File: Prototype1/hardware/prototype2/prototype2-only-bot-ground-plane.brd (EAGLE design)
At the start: 96.6 x 74.9 mm, 94 parts, among them IC1 ATTINY13A-SSU, IC2 LDL112D33R, IC3 FT2232HL-REEL, IC4 93LC46BT-I_OT, IC5 APA104, IC6 APA104, IC7 APA104, IC8 APA104, J4 DN PAIR, U2 ESP-WROOM-32

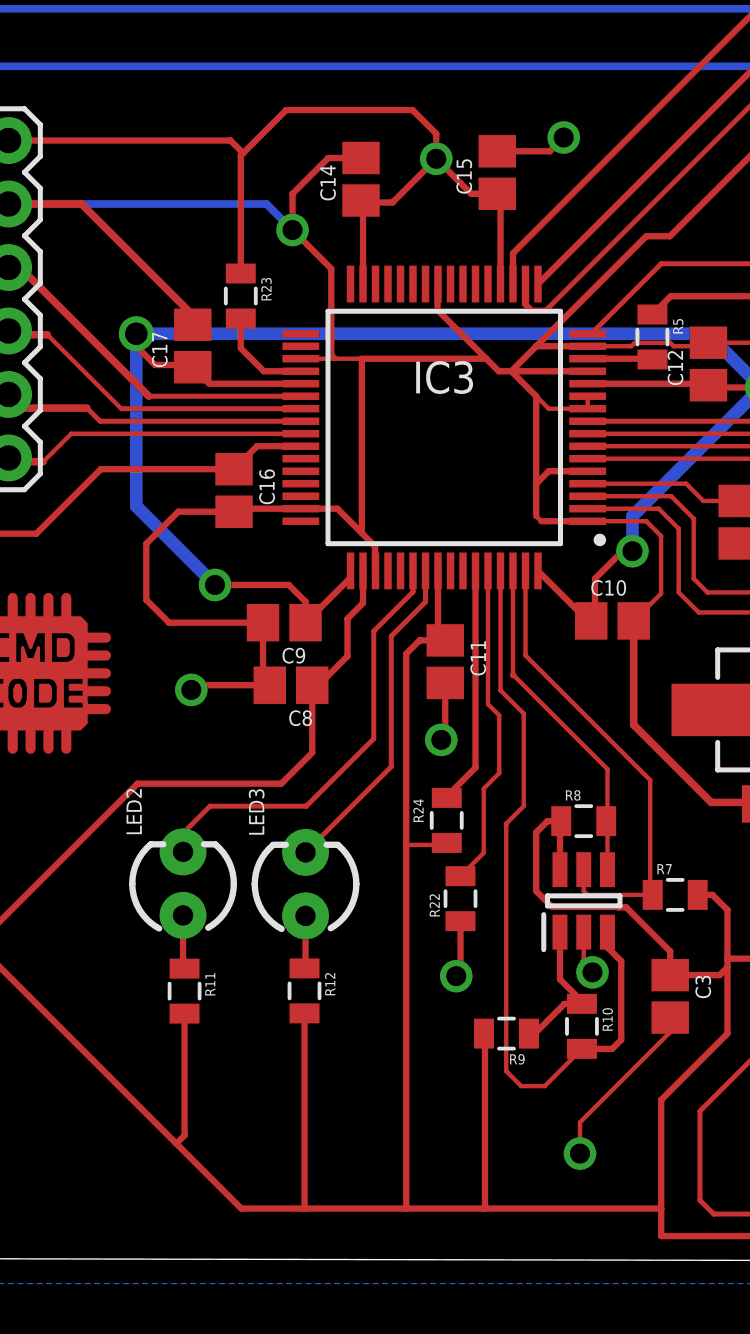
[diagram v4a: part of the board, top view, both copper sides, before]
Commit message: removed inputs to output pins....duh
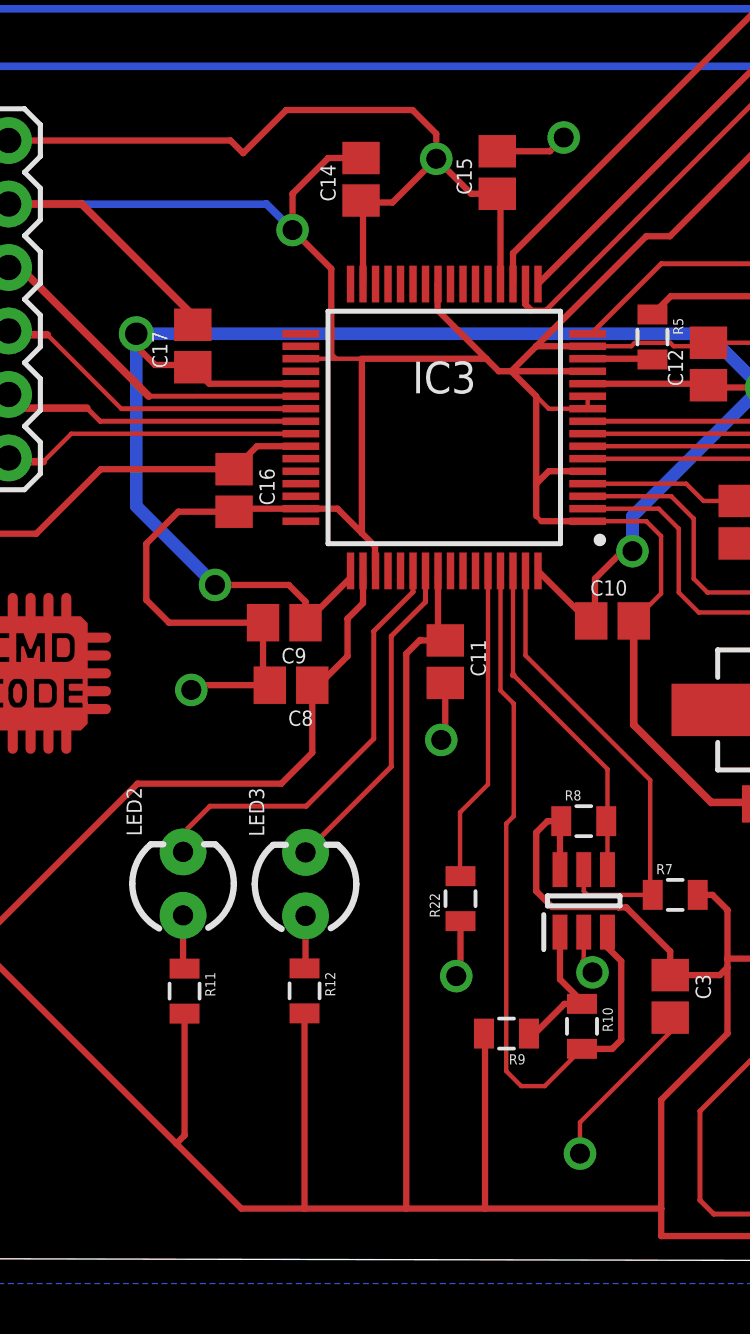
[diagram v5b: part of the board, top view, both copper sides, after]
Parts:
- removed R23, R24: 10 K, passives:0805
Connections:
- net PWRSAV: no longer R24.2
- net SUSPEND: no longer R23.2
- net VCC: no longer R23.1, R24.1
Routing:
- net PWRSAV: track 9.56 -> 0.00 mm
- net VCC: track 547.8 -> 541.3 mm
- net SUSPEND: track 3.97 -> 0.00 mm
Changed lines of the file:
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@@
 <attribute name="VALUE" x="26.367" y="14.384" size="0.4064" layer="27" rot="R90"/>
-</element>
-<element name="R23" library="passives" package="0805" value="10 K" x="16.18" y="39.51" smashed="yes" rot="R270">
-<attribute name="NAME" x="17.0055" y="40.272" size="0.4064" layer="25" rot="R270"/>
-<attribute name="VALUE" x="14.783" y="40.526" size="0.4064" layer="27" rot="R270"/>
-</element>
-<element name="R24" library="passives" package="0805" value="10 K" x="24.42" y="18.53" smashed="yes" rot="R90">
-<attribute name="NAME" x="23.4945" y="18.418" size="0.4064" layer="25" rot="R90"/>
-<attribute name="VALUE" x="25.817" y="17.514" size="0.4064" layer="27" rot="R90"/>
 </element>
 <element name="R3" library="passives" package="0805" value="20 R" x="87.8" y="22.05" smashed="yes" rot="R180">
@@
 <contactref element="EMIFILTER1" pad="1"/>
 <contactref element="EMIFILTER2" pad="1"/>
-<contactref element="R23" pad="1"/>
-<contactref element="R24" pad="1"/>
 <contactref element="IC4" pad="6"/>
 <contactref element="C3" pad="1"/>
@@
 <wire x1="23.37" y1="25.73" x2="23.35" y2="25.75" width="0.254" layer="1"/>
 <wire x1="23.35" y1="25.75" x2="22.8" y2="25.2" width="0.254" layer="1"/>
-<wire x1="22.8" y1="25.2" x2="22.8" y2="17.55" width="0.254" layer="1"/>
-<wire x1="22.8" y1="17.55" x2="22.8" y2="3" width="0.254" layer="1"/>
+<wire x1="22.8" y1="25.2" x2="22.8" y2="3" width="0.254" layer="1"/>
 <wire x1="19.04" y1="23.94" x2="19.04" y2="21.24" width="0.254" layer="1"/>
 <wire x1="17.8" y1="20" x2="12.05" y2="20" width="0.254" layer="1"/>
@@
 <wire x1="23.05" y1="46.95" x2="18" y2="46.95" width="0.254" layer="1"/>
 <wire x1="18" y1="46.95" x2="16.275" y2="45.225" width="0.254" layer="1"/>
-<wire x1="16.275" y1="45.225" x2="16.18" y2="45.13" width="0.254" layer="1"/>
-<wire x1="16.18" y1="45.13" x2="16.18" y2="40.41" width="0.254" layer="1"/>
 <wire x1="41.3" y1="73.43" x2="41.24" y2="73.37" width="0.254" layer="1"/>
 <wire x1="41.24" y1="73.37" x2="36.25" y2="73.37" width="0.254" layer="1"/>
@@
 <wire x1="83.75" y1="59.47" x2="80.93" y2="62.29" width="0.254" layer="1"/>
 <wire x1="80.93" y1="62.29" x2="80.93" y2="62.44" width="0.254" layer="1"/>
-<wire x1="24.42" y1="17.63" x2="24.34" y2="17.55" width="0.1778" layer="1"/>
-<wire x1="24.34" y1="17.55" x2="22.8" y2="17.55" width="0.1778" layer="1"/>
 <wire x1="35.65" y1="13" x2="43" y2="13" width="0.254" layer="1"/>
 <wire x1="50" y1="20" x2="50" y2="25" width="0.254" layer="1"/>
@@
 <wire x1="50.3" y1="67" x2="50.3" y2="74.4" width="0.508" layer="1"/>
 <wire x1="50.3" y1="74.4" x2="50" y2="74.7" width="0.508" layer="1"/>
-<wire x1="34.55" y1="73.37" x2="41.3" y2="74.7" width="0" layer="19" extent="1-1"/>
-<wire x1="60.12" y1="45.6361" x2="70.65875" y2="46.085" width="0" layer="19" extent="1-1"/>
-<wire x1="44.69" y1="36.39" x2="54.78" y2="41.5" width="0" layer="19" extent="1-1"/>
-<wire x1="36.04" y1="29.61" x2="32.9944" y2="29.9056" width="0" layer="19" extent="1-1"/>
-<wire x1="33.36" y1="10.06" x2="34.55" y2="6.9" width="0" layer="19" extent="1-1"/>
-<wire x1="30.25" y1="12.45" x2="33.36" y2="10.64" width="0" layer="19" extent="1-1"/>
-<wire x1="24.97" y1="12.47" x2="29.85" y2="12.9" width="0" layer="19" extent="1-1"/>
-<wire x1="28.55" y1="45.3" x2="32.4" y2="41.9" width="0" layer="19" extent="1-1"/>
-<wire x1="24.36" y1="24.03" x2="21.57" y2="28.512" width="0" layer="19" extent="1-1"/>
-<wire x1="70.11" y1="5.9" x2="63.27" y2="4.74" width="0" layer="19" extent="1-1"/>
-<wire x1="28.12" y1="58.61" x2="29.1" y2="45.85" width="0" layer="19" extent="1-1"/>
 </signal>
 <signal name="DISPLAY_CS" airwireshidden="yes">
@@
 <contactref element="IC3" pad="61"/>
 <wire x1="26.57" y1="28.512" x2="26.57" y2="23.73" width="0.1778" layer="1"/>
-<wire x1="26.57" y1="23.73" x2="27.5" y2="22.8" width="0.1778" layer="1"/>
-<wire x1="27.5" y1="22.8" x2="27.5" y2="19.1" width="0.1778" layer="1"/>
-<wire x1="27.5" y1="19.1" x2="26.8" y2="18.4" width="0.1778" layer="1"/>
+<wire x1="26.57" y1="23.73" x2="27.1" y2="23.2" width="0.1778" layer="1"/>
+<wire x1="27.1" y1="23.2" x2="27.1" y2="18.7" width="0.1778" layer="1"/>
+<wire x1="27.1" y1="18.7" x2="26.8" y2="18.4" width="0.1778" layer="1"/>
 <wire x1="26.8" y1="18.4" x2="26.8" y2="8.5" width="0.1778" layer="1"/>
 <wire x1="26.8" y1="8.5" x2="27.4" y2="7.9" width="0.1778" layer="1"/>
@@
 <contactref element="IC3" pad="60"/>
 <contactref element="R22" pad="2"/>
-<wire x1="26.07" y1="28.512" x2="26.07" y2="23.18" width="0.1778" layer="1"/>
-<wire x1="26.52" y1="22.73" x2="26.07" y2="23.18" width="0.1778" layer="1"/>
-<wire x1="25.9" y1="17.23" x2="24.97" y2="16.3" width="0.1778" layer="1"/>
-<wire x1="25.9" y1="19.8" x2="26.52" y2="20.42" width="0.1778" layer="1"/>
-<wire x1="25.9" y1="19.8" x2="25.9" y2="17.23" width="0.1778" layer="1"/>
-<wire x1="26.52" y1="20.42" x2="26.52" y2="22.73" width="0.1778" layer="1"/>
+<wire x1="24.95" y1="18.85" x2="26.07" y2="19.97" width="0.1778" layer="1"/>
+<wire x1="24.95" y1="18.85" x2="24.95" y2="16.32" width="0.1778" layer="1"/>
+<wire x1="24.97" y1="16.3" x2="24.95" y2="16.32" width="0.1778" layer="1"/>
+<wire x1="26.07" y1="19.97" x2="26.07" y2="28.512" width="0.1778" layer="1"/>
 </signal>
 <signal name="SUSPEND" airwireshidden="yes">
 <contactref element="IC3" pad="36"/>
-<contactref element="R23" pad="2"/>
-<wire x1="18.582" y1="36.5" x2="17.1" y2="36.5" width="0.254" layer="1"/>
-<wire x1="16.18" y1="37.42" x2="16.18" y2="38.61" width="0.254" layer="1"/>
-<wire x1="17.1" y1="36.5" x2="16.18" y2="37.42" width="0.254" layer="1"/>
 </signal>
 <signal name="PWRSAV" airwireshidden="yes">
 <contactref element="IC3" pad="59"/>
-<contactref element="R24" pad="2"/>
-<wire x1="25.57" y1="20.63865" x2="24.42" y2="19.48865" width="0.254" layer="1"/>
-<wire x1="24.42" y1="19.43" x2="24.42" y2="19.48865" width="0.254" layer="1"/>
-<wire x1="25.57" y1="20.63865" x2="25.57" y2="28.512" width="0.254" layer="1"/>
 </signal>
 <signal name="RXD_SPI_PROM_MOSI" airwireshidden="yes">
